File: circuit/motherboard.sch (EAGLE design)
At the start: 3 parts

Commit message: Think I've got the circuitry down, boarding next
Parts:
- added R1: (no value), adafruit:FLIPFLOP-RES
- added S1, S2, S3, S4: (no value), switch-omron:10-XX
- added S5: (no value), switch:255SB
- added T1: BC337, transistor:BC337
- added U$3: BATTERY-CHARGER-LI-PROT, diy-modules:BATTERY-CHARGER-LI-PROT
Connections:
- new net N$10: DIS1.DIN, U$1.D3
- new net N$11: DIS1.CD, U$1.D4
- new net N$12: DIS1.CE, U$1.D5
- new net N$13: DIS1.RST, U$1.D7
- new net N$14: R1.1, U$1.D6
- new net N$15: S5.P, U$3.OUT+
- new net N$16: R1.2, T1.B
- new net N$17: DIS1.BL, T1.C
- new net N$18: S4.S, S4.S1, U$1.A0
- new net N$19: S3.S, S3.S1, U$1.A1
- new net N$20: S2.S, S2.S1, U$1.A2
- new net N$21: S1.S, S1.S1, U$1.A3
- new net N$22: DIS1.GND, S1.P, S2.P, S3.P, S4.P, U$1.GND, U$3.OUT-
- new net N$23: S5.S, U$1.5.5V
- new net N$9: DIS1.CLK, U$1.D2
- net N$1: now also DIS1.VCC
- net N$3: now also T1.E
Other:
- moved on the sheet: DIS1

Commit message: PCB coming along nicely
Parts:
- removed DIS1: NOKIA5110, _LCD_Nokia5110:NOKIA5110
- removed S5: (no value), switch:255SB
- removed U$2: AI-THINKER_RA-01, LoRa_modules:AI-THINKER_RA-01
- added DIS2: NOKIA5110, _LCD_Nokia5110-minimal:NOKIA5110
- added JP1: (no value), pinhead:PINHD-1X2/90
- added R2, R3: 10k, adafruit:FLIPFLOP-RES
- added U$4: AI-THINKER_RA-01, lora-ra-02-minimal-because-labels-fuckup-rotating:AI-THINKER_RA-01
- R1: value (none) -> 10k
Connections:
- removed net N$14: R1.1, U$1.D6
- removed net N$15: S5.P, U$3.OUT+
- removed net N$22: DIS1.GND, S1.P, S2.P, S3.P, S4.P, U$1.GND, U$3.OUT-
- removed net N$23: S5.S, U$1.5.5V
- new net +3V3: DIS2.VCC, U$1.3.3V, U$4.3.3V
- new net +5V: U$1.5.5V, U$3.OUT+
- new net GND: DIS2.GND, JP1.2, R2.2, S1.P, S2.P, S3.P, S4.P, T1.E, U$1.GND2, U$4.GND@2
- new net N$24: R2.1, R3.2, U$1.A7
- new net N$25: R3.1, U$3.B+
- net N$1: now also JP1.1, U$3.OUT-; no longer DIS1.VCC, U$1.3.3V, U$2.3.3V
- net N$10: now also DIS2.DIN, U$1.D6; no longer DIS1.DIN, U$1.D3
- net N$11: now also DIS2.CD, U$1.D5; no longer DIS1.CD, U$1.D4
- net N$12: now also DIS2.CE, U$1.D4; no longer DIS1.CE, U$1.D5
- net N$13: now also R1.1, U$1.D3; no longer DIS1.RST, U$1.D7
- net N$17: now also DIS2.BL; no longer DIS1.BL
- net N$2: now also U$4.SCK; no longer U$2.SCK
- net N$3: now also DIS2.CLK, U$1.D7; no longer T1.E, U$1.GND2, U$2.GND@2
- net N$4: now also U$4.MISO; no longer U$2.MISO
- net N$5: now also U$4.MOSI; no longer U$2.MOSI
- net N$6: now also U$4.NSS; no longer U$2.NSS
- net N$7: now also U$4.DIO0; no longer U$2.DIO0
- net N$8: now also U$4.RESET; no longer U$2.RESET
- net N$9: now also DIS2.RST; no longer DIS1.CLK
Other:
- moved on the sheet: U$3

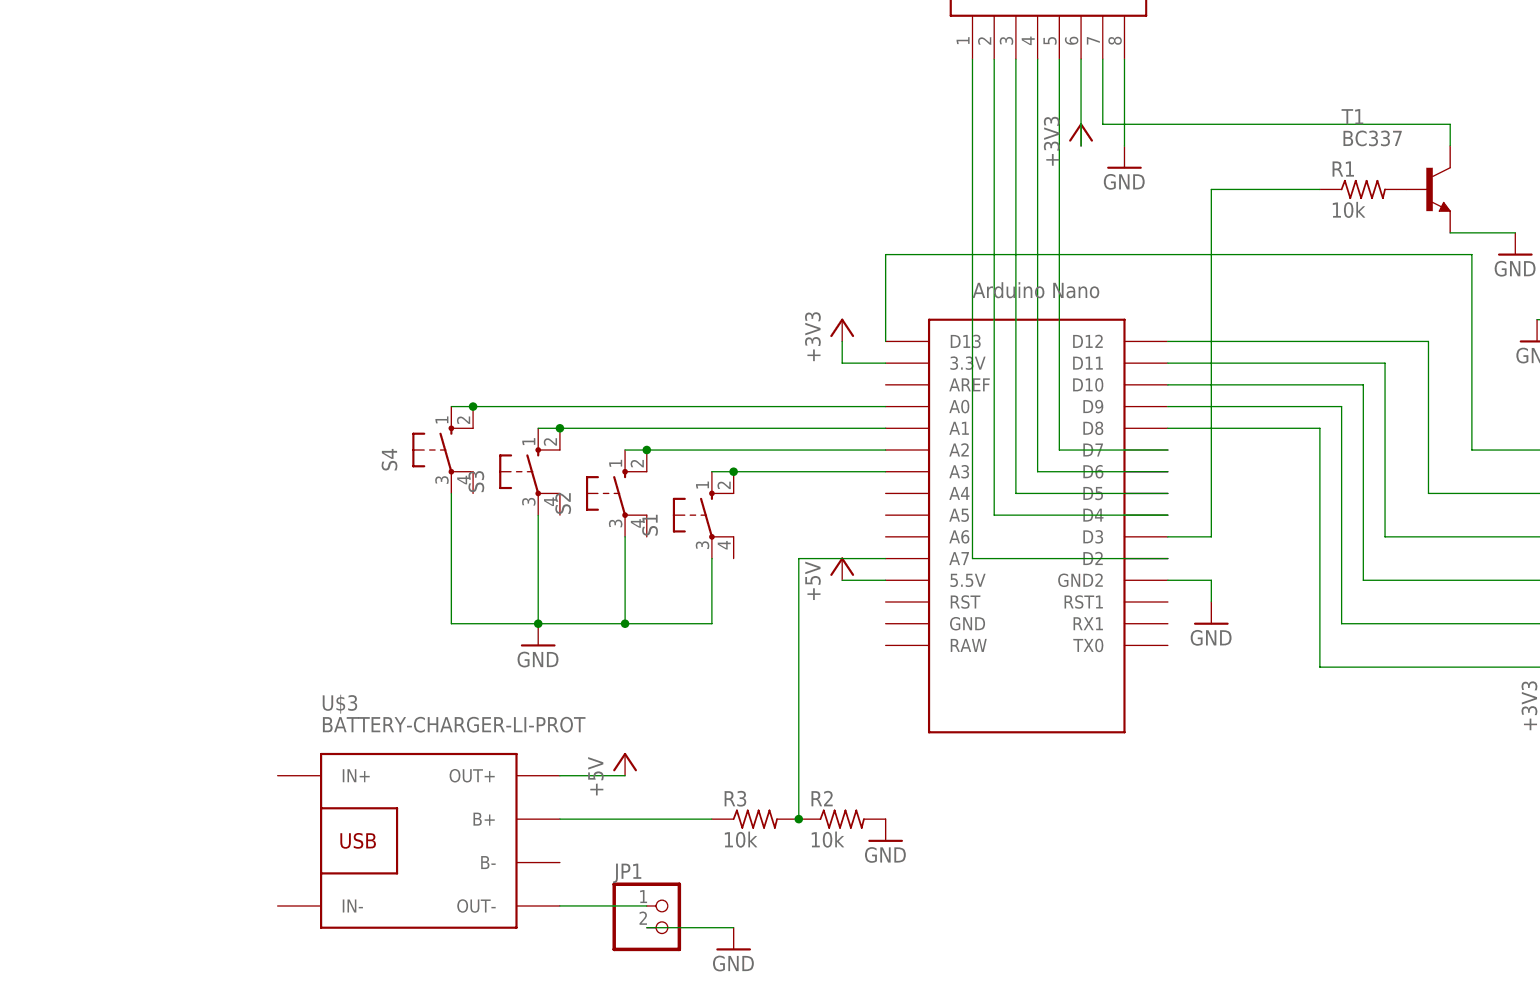
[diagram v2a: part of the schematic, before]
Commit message: Finished the PCB.. and then decided I should split the display/buttons separately
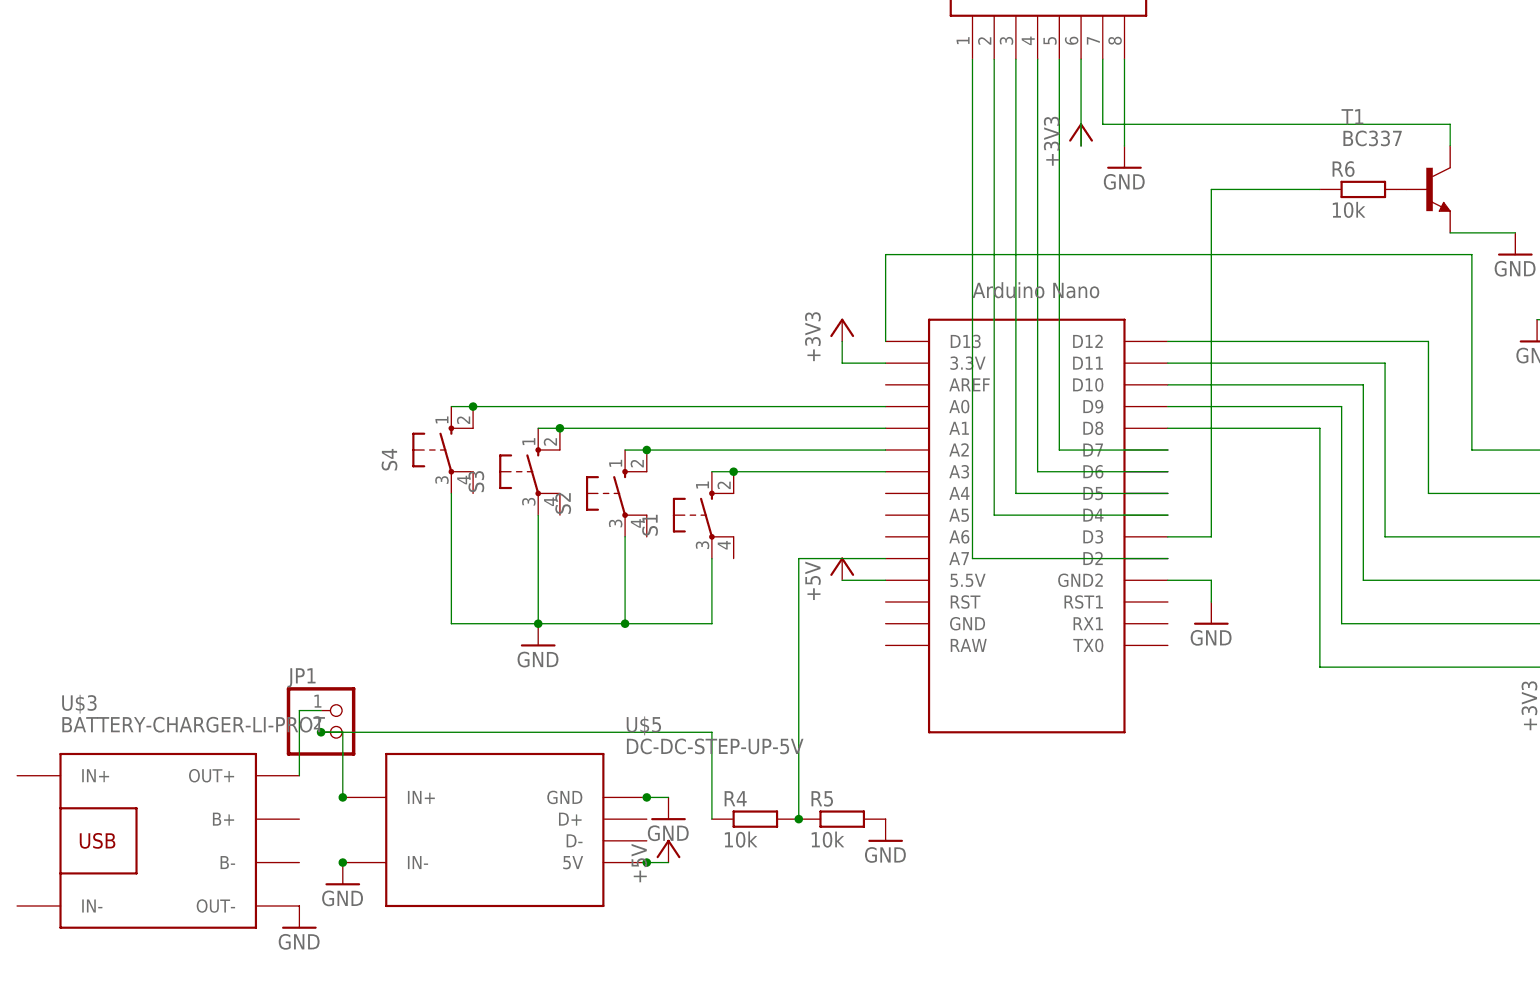
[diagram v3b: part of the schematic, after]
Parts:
- removed R1, R2, R3: 10k, adafruit:FLIPFLOP-RES
- added R4, R5, R6: 10k, rcl:R-EU_0204/5
- added U$5: DC-DC-STEP-UP-5V, 5v-step-up-minimal:DC-DC-STEP-UP-5V
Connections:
- removed net N$25: R3.1, U$3.B+
- new net N$14: R6.2, T1.B
- new net N$15: JP1.1, U$3.OUT+
- net +5V: now also U$5.5V; no longer U$3.OUT+
- net GND: now also R5.2, U$5.GND, U$5.IN-; no longer JP1.2, R2.2
- net N$1: no longer JP1.1
- net N$13: now also R6.1; no longer R1.1
- net N$16: now also JP1.2, R4.1, U$5.IN+; no longer R1.2, T1.B
- net N$24: now also R4.2, R5.1; no longer R2.1, R3.2
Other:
- moved on the sheet: JP1, U$3

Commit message: Getting to be quite a serious design..
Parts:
- added J1, J2: XF2L-2235-1, con-omron:XF2L-2235-1
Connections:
- removed net N$16: JP1.2, R4.1, U$5.IN+
- new net N$17: DIS2.RST, J2-9.MS
- new net N$22: J2-12.MS, S3.P
- new net N$25: DIS2.VCC, J2-3.MS
- new net N$26: DIS2.CLK, J2-4.MS
- new net N$27: DIS2.DIN, J2-5.MS
- new net N$28: DIS2.CD, J2-6.MS
- new net N$29: DIS2.CE, J2-7.MS
- new net N$30: J2-13.MS, S4.P
- new net N$32: J1-13.MS, U$1.A0
- new net N$33: J1-12.MS, U$1.A1
- new net N$34: J1-11.MS, U$1.A2
- new net N$35: J1-10.MS, U$1.A3
- net +3V3: now also J1-20.MS; no longer DIS2.VCC
- net GND: now also J1-22.MS, J2-1.MSV, S1.S, S1.S1, S2.S, S2.S1, S3.S, S3.S1, S4.S, S4.S1; no longer S1.P, S2.P, S3.P, S4.P
- net N$10: now also J1-18.MS; no longer DIS2.DIN
- net N$11: now also J1-17.MS; no longer DIS2.CD
- net N$12: now also J1-16.MS; no longer DIS2.CE
- net N$13: now also J1-15.MS; no longer R6.1
- net N$15: now also JP1.2; no longer JP1.1
- net N$18: now also JP1.1, R4.1, U$5.IN+; no longer S4.S, S4.S1, U$1.A0
- net N$19: now also J2-8.MS, R6.1; no longer S3.S, S3.S1, U$1.A1
- net N$20: now also J2-10.MS, S1.P; no longer S2.S, S2.S1, U$1.A2
- net N$21: now also J2-11.MS, S2.P; no longer S1.S, S1.S1, U$1.A3
- net N$3: now also J1-19.MS; no longer DIS2.CLK
- net N$9: now also J1-14.MS; no longer DIS2.RST
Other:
- moved on the sheet: DIS2, R6, S1, S2, S3, S4, T1

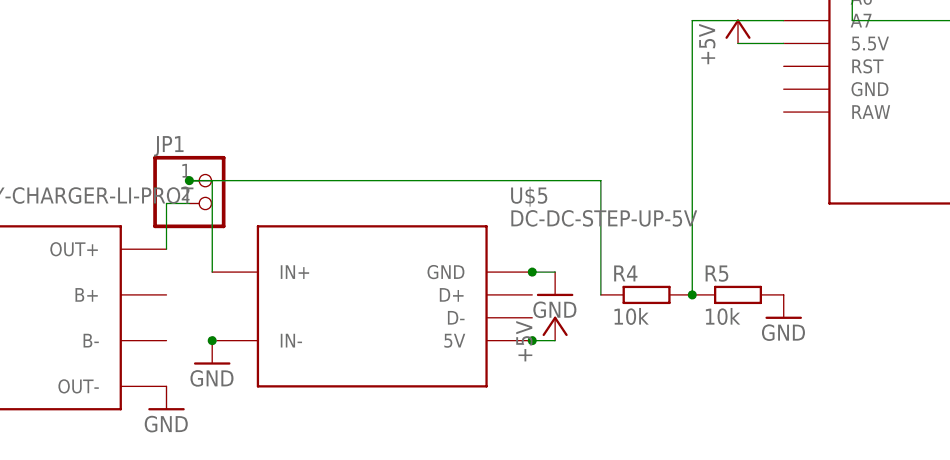
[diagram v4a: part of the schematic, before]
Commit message: Library parts are annoying
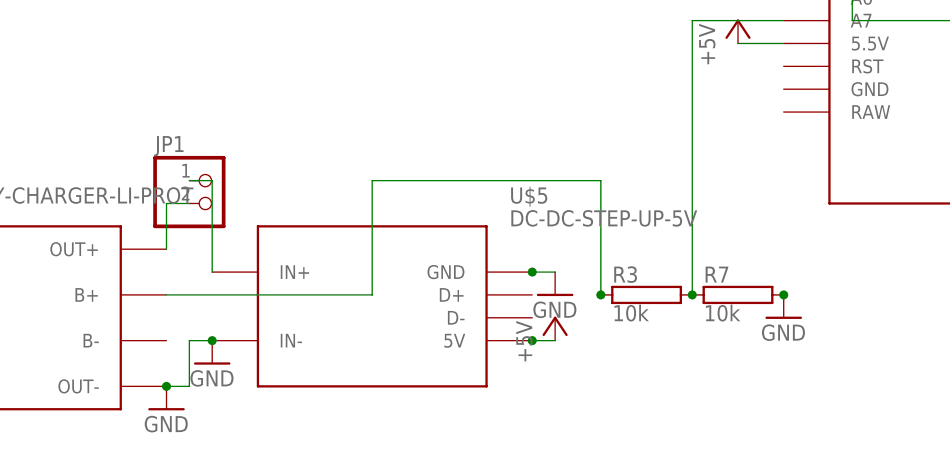
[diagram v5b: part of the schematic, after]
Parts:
- removed R4, R5: 10k, rcl:R-EU_0204/5
- added R3, R7: 10k, resistor-power:RAC01
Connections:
- removed net N$18: JP1.1, R4.1, U$5.IN+
- new net N$16: R3.1, U$3.B+
- net GND: now also R7.2, U$3.OUT-; no longer R5.2
- net N$1: now also JP1.1, U$5.IN+; no longer U$3.OUT-
- net N$24: now also R3.2, R7.1; no longer R4.2, R5.1

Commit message: Motherboard complete!
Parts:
- U$1: device Arduino-clone:NANO -> Arduino-clone-nano-minimal:NANO
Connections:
- net GND: now also U$4.GND@0
- net N$1: now also U$3.OUT+; no longer U$5.IN+
- net N$15: now also U$5.IN+; no longer U$3.OUT+
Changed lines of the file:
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@@
 <grid distance="0.1" unitdist="inch" unit="inch" style="lines" multiple="1" display="yes" altdistance="0.01" altunitdist="inch" altunit="inch"/>
 <layers>
-<layer number="1" name="Top" color="4" fill="1" visible="no" active="no"/>
-<layer number="16" name="Bottom" color="1" fill="1" visible="no" active="no"/>
-<layer number="17" name="Pads" color="2" fill="1" visible="no" active="no"/>
-<layer number="18" name="Vias" color="2" fill="1" visible="no" active="no"/>
-<layer number="19" name="Unrouted" color="6" fill="1" visible="no" active="no"/>
-<layer number="20" name="Dimension" color="24" fill="1" visible="no" active="no"/>
-<layer number="21" name="tPlace" color="7" fill="1" visible="no" active="no"/>
-<layer number="22" name="bPlace" color="7" fill="1" visible="no" active="no"/>
-<layer number="23" name="tOrigins" color="15" fill="1" visible="no" active="no"/>
-<layer number="24" name="bOrigins" color="15" fill="1" visible="no" active="no"/>
-<layer number="25" name="tNames" color="7" fill="1" visible="no" active="no"/>
-<layer number="26" name="bNames" color="7" fill="1" visible="no" active="no"/>
-<layer number="27" name="tValues" color="7" fill="1" visible="no" active="no"/>
-<layer number="28" name="bValues" color="7" fill="1" visible="no" active="no"/>
+<layer number="1" name="Top" color="4" fill="1" visible="yes" active="no"/>
+<layer number="16" name="Bottom" color="1" fill="1" visible="yes" active="no"/>
+<layer number="17" name="Pads" color="2" fill="1" visible="yes" active="no"/>
+<layer number="18" name="Vias" color="2" fill="1" visible="yes" active="no"/>
+<layer number="19" name="Unrouted" color="6" fill="1" visible="yes" active="no"/>
+<layer number="20" name="Dimension" color="24" fill="1" visible="yes" active="no"/>
+<layer number="21" name="tPlace" color="7" fill="1" visible="yes" active="no"/>
+<layer number="22" name="bPlace" color="7" fill="1" visible="yes" active="no"/>
+<layer number="23" name="tOrigins" color="15" fill="1" visible="yes" active="no"/>
+<layer number="24" name="bOrigins" color="15" fill="1" visible="yes" active="no"/>
+<layer number="25" name="tNames" color="7" fill="1" visible="yes" active="no"/>
+<layer number="26" name="bNames" color="7" fill="1" visible="yes" active="no"/>
+<layer number="27" name="tValues" color="7" fill="1" visible="yes" active="no"/>
+<layer number="28" name="bValues" color="7" fill="1" visible="yes" active="no"/>
 <layer number="29" name="tStop" color="7" fill="3" visible="no" active="no"/>
 <layer number="30" name="bStop" color="7" fill="6" visible="no" active="no"/>
@@
 <layer number="35" name="tGlue" color="7" fill="4" visible="no" active="no"/>
 <layer number="36" name="bGlue" color="7" fill="5" visible="no" active="no"/>
-<layer number="37" name="tTest" color="7" fill="1" visible="no" active="no"/>
-<layer number="38" name="bTest" color="7" fill="1" visible="no" active="no"/>
+<layer number="37" name="tTest" color="7" fill="1" visible="yes" active="no"/>
+<layer number="38" name="bTest" color="7" fill="1" visible="yes" active="no"/>
 <layer number="39" name="tKeepout" color="4" fill="11" visible="no" active="no"/>
 <layer number="40" name="bKeepout" color="1" fill="11" visible="no" active="no"/>
@@
 <layer number="44" name="Drills" color="7" fill="1" visible="no" active="no"/>
 <layer number="45" name="Holes" color="7" fill="1" visible="no" active="no"/>
-<layer number="46" name="Milling" color="3" fill="1" visible="no" active="no"/>
-<layer number="47" name="Measures" color="7" fill="1" visible="no" active="no"/>
-<layer number="48" name="Document" color="7" fill="1" visible="no" active="no"/>
-<layer number="49" name="Reference" color="7" fill="1" visible="no" active="no"/>
-<layer number="50" name="dxf" color="7" fill="1" visible="no" active="no"/>
-<layer number="51" name="tDocu" color="7" fill="1" visible="no" active="no"/>
-<layer number="52" name="bDocu" color="7" fill="1" visible="no" active="no"/>
-<layer number="53" name="tGND_GNDA" color="7" fill="9" visible="no" active="no"/>
-<layer number="54" name="bGND_GNDA" color="1" fill="9" visible="no" active="no"/>
-<layer number="56" name="wert" color="7" fill="1" visible="no" active="no"/>
-<layer number="57" name="tCAD" color="7" fill="1" visible="no" active="no"/>
-<layer number="59" name="tCarbon" color="7" fill="1" visible="no" active="no"/>
-<layer number="60" name="bCarbon" color="7" fill="1" visible="no" active="no"/>
+<layer number="46" name="Milling" color="3" fill="1" visible="yes" active="no"/>
+<layer number="47" name="Measures" color="7" fill="1" visible="yes" active="no"/>
+<layer number="48" name="Document" color="7" fill="1" visible="yes" active="no"/>
+<layer number="49" name="Reference" color="7" fill="1" visible="yes" active="no"/>
+<layer number="50" name="dxf" color="7" fill="1" visible="yes" active="no"/>
+<layer number="51" name="tDocu" color="7" fill="1" visible="yes" active="no"/>
+<layer number="52" name="bDocu" color="7" fill="1" visible="yes" active="no"/>
+<layer number="53" name="tGND_GNDA" color="7" fill="9" visible="yes" active="no"/>
+<layer number="54" name="bGND_GNDA" color="1" fill="9" visible="yes" active="no"/>
+<layer number="56" name="wert" color="7" fill="1" visible="yes" active="no"/>
+<layer number="57" name="tCAD" color="7" fill="1" visible="yes" active="no"/>
+<layer number="59" name="tCarbon" color="7" fill="1" visible="yes" active="no"/>
+<layer number="60" name="bCarbon" color="7" fill="1" visible="yes" active="no"/>
 <layer number="88" name="SimResults" color="9" fill="1" visible="yes" active="yes"/>
 <layer number="89" name="SimProbes" color="9" fill="1" visible="yes" active="yes"/>
@@
 </classes>
 <parts>
-<part name="U$1" library="Arduino-clone" deviceset="NANO" device=""/>
+<part name="U$1" library="Arduino-clone-nano-minimal" deviceset="NANO" device=""/>
 <part name="T1" library="transistor" library_urn="urn:adsk.eagle:library:402" deviceset="BC337" device="" package3d_urn="urn:adsk.eagle:package:28523/2"/>
 <part name="S1" library="switch-omron" library_urn="urn:adsk.eagle:library:377" deviceset="10-XX" device="" package3d_urn="urn:adsk.eagle:package:27496/1"/>
@@
 <part name="R3" library="resistor-power" library_urn="urn:adsk.eagle:library:344" deviceset="R" device="AC01" package3d_urn="urn:adsk.eagle:package:25124/1" value="10k"/>
 <part name="R7" library="resistor-power" library_urn="urn:adsk.eagle:library:344" deviceset="R" device="AC01" package3d_urn="urn:adsk.eagle:package:25124/1" value="10k"/>
+<part name="GND7" library="supply1" library_urn="urn:adsk.eagle:library:371" deviceset="GND" device=""/>
 </parts>
 <sheets>
@@
 <attribute name="VALUE" x="29.21" y="12.319" size="1.778" layer="96"/>
 </instance>
+<instance part="GND7" gate="1" x="175.26" y="30.48" smashed="yes">
+<attribute name="VALUE" x="172.72" y="27.94" size="1.778" layer="96"/>
+</instance>
 </instances>
 <busses>
@@
 <junction x="38.1" y="15.24"/>
 </segment>
+<segment>
+<pinref part="U$4" gate="P$1" pin="GND@0"/>
+<pinref part="GND7" gate="1" pin="GND"/>
+<wire x1="170.18" y1="33.02" x2="175.26" y2="33.02" width="0.1524" layer="91"/>
+</segment>
 </net>
 <net name="N$9" class="0">
@@
 <wire x1="20.32" y1="93.98" x2="20.32" y2="55.88" width="0.1524" layer="91"/>
 <wire x1="20.32" y1="55.88" x2="38.1" y2="55.88" width="0.1524" layer="91"/>
-</segment>
-</net>
-<net name="N$15" class="0">
-<segment>
-<pinref part="U$3" gate="G$1" pin="OUT+"/>
-<pinref part="JP1" gate="G$1" pin="2"/>
-<wire x1="-30.48" y1="20.32" x2="-30.48" y2="25.4" width="0.1524" layer="91"/>
-<wire x1="-30.48" y1="25.4" x2="-27.94" y2="25.4" width="0.1524" layer="91"/>
-</segment>
-</net>
-<net name="N$1" class="0">
-<segment>
-<pinref part="U$5" gate="G$1" pin="IN+"/>
-<wire x1="-25.4" y1="27.94" x2="-25.4" y2="17.78" width="0.1524" layer="91"/>
-<pinref part="JP1" gate="G$1" pin="1"/>
-<wire x1="-27.94" y1="27.94" x2="-25.4" y2="27.94" width="0.1524" layer="91"/>
 </segment>
 </net>
@@
 </segment>
 </net>
+<net name="N$1" class="0">
+<segment>
+<pinref part="U$3" gate="G$1" pin="OUT+"/>
+<pinref part="JP1" gate="G$1" pin="1"/>
+<wire x1="-30.48" y1="20.32" x2="-30.48" y2="27.94" width="0.1524" layer="91"/>
+<wire x1="-30.48" y1="27.94" x2="-27.94" y2="27.94" width="0.1524" layer="91"/>
+</segment>
+</net>
+<net name="N$15" class="0">
+<segment>
+<pinref part="JP1" gate="G$1" pin="2"/>
+<wire x1="-27.94" y1="25.4" x2="-27.94" y2="17.78" width="0.1524" layer="91"/>
+<pinref part="U$5" gate="G$1" pin="IN+"/>
+<wire x1="-27.94" y1="17.78" x2="-25.4" y2="17.78" width="0.1524" layer="91"/>
+</segment>
+</net>
